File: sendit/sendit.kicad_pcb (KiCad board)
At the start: 4 copper layers, 160.7 x 51.7 mm, 227 parts, among them J1 Conn_01x04_MountingPin, J10 USB_TYPE_C_16PIN, J14 Conn_02x05_Odd_Even, J16 Conn_02x05_Odd_Even, J2 Conn_02x09_Odd_Even, J21 Conn_02x05_Odd_Even, J23 Conn_02x05_Odd_Even, J27 Conn_02x05_Odd_Even, J29 Conn_02x05_Odd_Even, J34 Conn_02x05_Odd_Even, J36 Conn_02x05_Odd_Even, J42 Conn_02x05_Odd_Even, J44 Conn_02x05_Odd_Even, J49 Conn_02x05_Odd_Even, J51 Conn_02x05_Odd_Even, J56 Conn_02x05_Odd_Even, J58 Conn_02x05_Odd_Even, J6 Conn_02x05_Odd_Even, J8 Conn_02x05_Odd_Even, Q1 AO3400A, SW1 RESET, SW2 BOOT, U1 ESP32-S3-WROOM-1-N16R8, U2 USBLC6-2SC6, U3 SN74LV1T34DBV, U4 XC6210B332MR, U5 ADS1115IDGSR, U6 ADS1115IDGSR, U7 TPS7A2033PDBVR, U8 MT3608, U9 AP63205WU

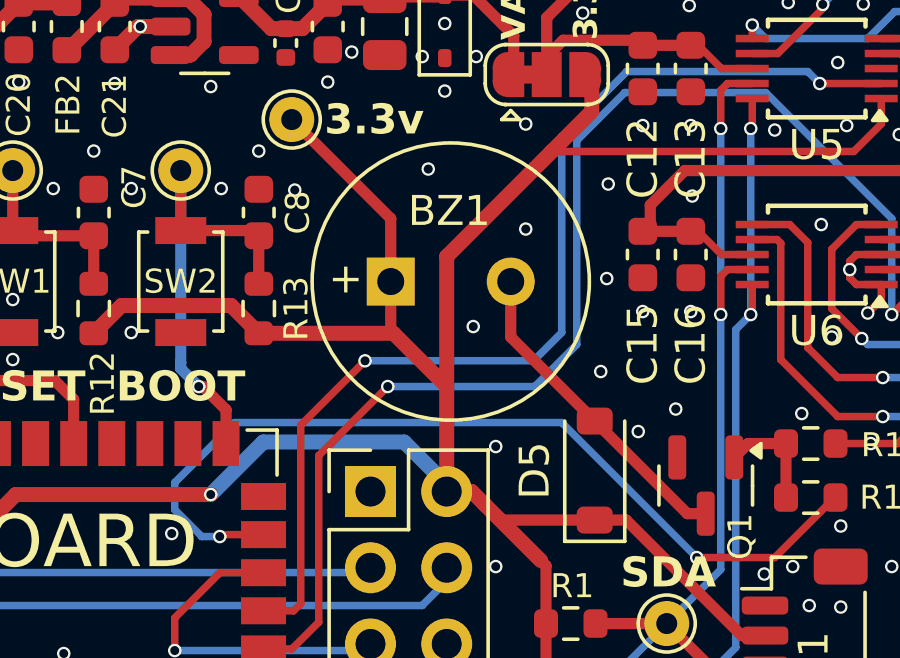
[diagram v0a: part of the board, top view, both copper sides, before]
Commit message: all footprints have 3d models now
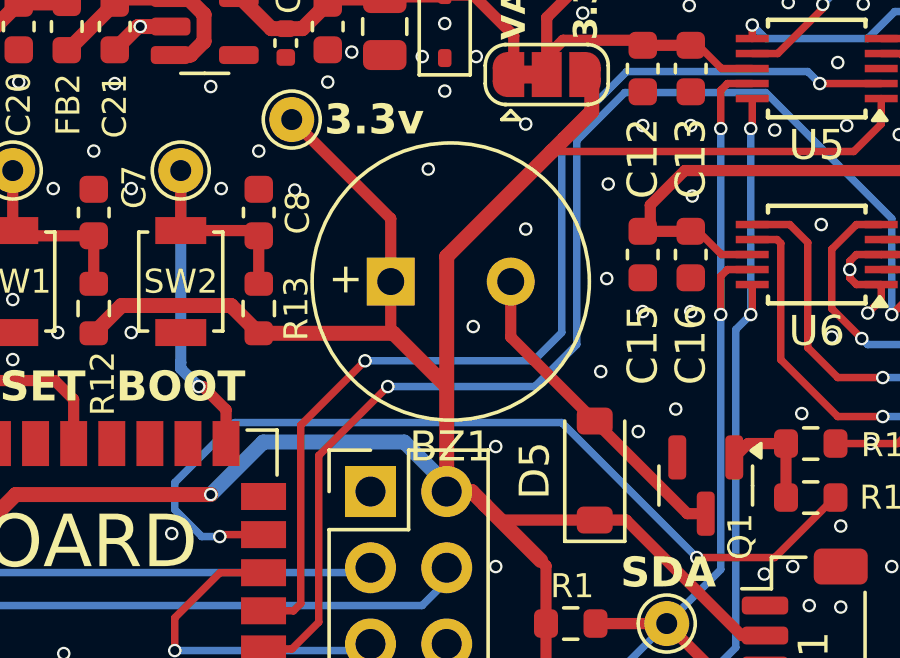
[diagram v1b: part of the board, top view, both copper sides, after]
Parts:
- BZ1: footprint Buzzer_Beeper:MagneticBuzzer_PUI_AT-0927-TT-6-R -> yarrboard:MagneticBuzzer_QMB-09B-03
- moved BZ1 2.00 mm to (91.5, 86.0)
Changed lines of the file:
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@@
 		)
 	)
-	(footprint "Buzzer_Beeper:MagneticBuzzer_PUI_AT-0927-TT-6-R"
+	(footprint "yarrboard:MagneticBuzzer_QMB-09B-03"
 		(layer "F.Cu")
-		(at 89.5 86)
+		(at 91.5 86)
 		(descr "Buzzer Magnetic 9mm AT-0927-TT-6-R, http://www.puiaudio.com/pdf/AT-0927-TT-6-R.pdf")
 		(tags "Buzzer Magnetic 9mm AT-0927-TT-6-R")
 		(property "Reference" "BZ1"
-			(at 1.95 -2.35 0)
+			(at 0 5.5 0)
 			(layer "F.SilkS")
 			(effects
@@
 		)
 		(property "Value" "Buzzer"
-			(at 2 7 0)
+			(at 0 7 0)
 			(layer "F.Fab")
 			(effects
@@
 		(attr through_hole)
 		(fp_circle
-			(center 2 0)
-			(end 6.62 0)
+			(center 0 0)
+			(end 4.62 0)
 			(stroke
 				(width 0.12)
@@
 		)
 		(fp_circle
-			(center 2 0)
-			(end 6.75 0)
+			(center 0 0)
+			(end 4.75 0)
 			(stroke
 				(width 0.05)
@@
 		)
 		(fp_circle
-			(center 2 0)
-			(end 6.5 0)
+			(center 0 0)
+			(end 4.5 0)
 			(stroke
 				(width 0.1)
@@
 		)
 		(fp_text user "+"
-			(at -1.5 -0.1 0)
+			(at -3.5 -0.1 0)
 			(layer "F.SilkS")
 			(effects
@@
 		)
 		(fp_text user "+"
-			(at -1.5 -0.1 0)
+			(at -3.5 -0.1 0)
 			(layer "F.Fab")
 			(effects
@@
 		)
 		(fp_text user "${REFERENCE}"
-			(at 2 2 0)
+			(at 0 2 0)
 			(layer "F.Fab")
 			(effects
@@
 		)
 		(pad "1" thru_hole rect
-			(at 0 0)
+			(at -2 0)
 			(size 1.6 1.6)
 			(drill 0.9)
@@
 		)
 		(pad "2" thru_hole circle
-			(at 4 0)
+			(at 2 0)
 			(size 1.6 1.6)
 			(drill 0.9)
@@
 		)
 		(embedded_fonts no)
-		(model "${KICAD9_3DMODEL_DIR}/Buzzer_Beeper.3dshapes/MagneticBuzzer_PUI_AT-0927-TT-6-R.step"
+		(model "/Users/hoeken/github/yarrboard-hardware/models/Huaneng QMB-09B-03.step"
 			(offset
 				(xyz 0 0 0)

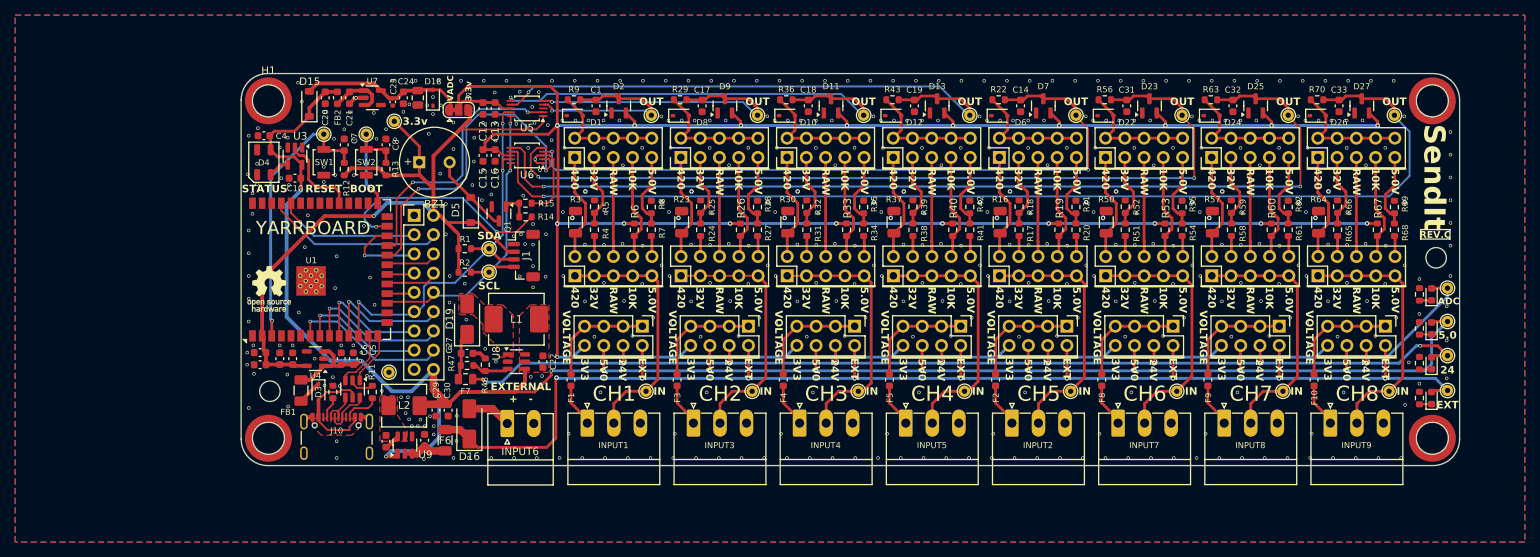
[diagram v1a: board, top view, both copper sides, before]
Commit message: moved the dc buck circuit away from the usb port.
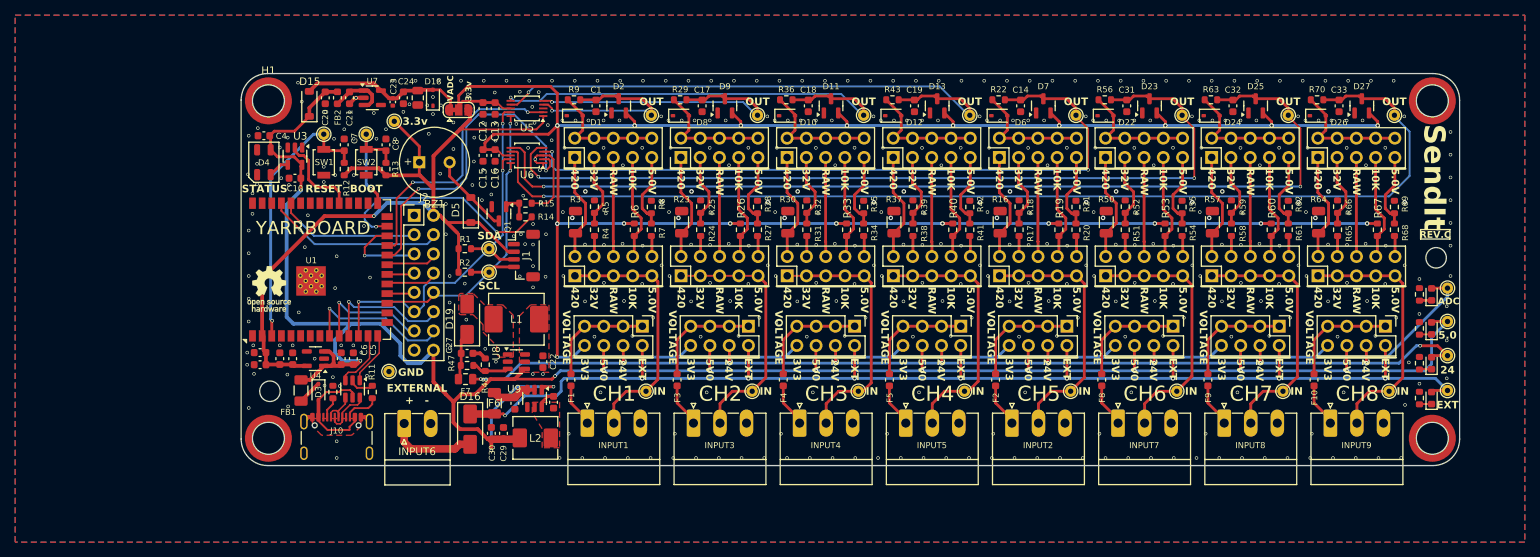
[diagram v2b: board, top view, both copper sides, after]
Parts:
- J2: footprint Connector_PinHeader_2.54mm:PinHeader_2x09_P2.54mm_Vertical -> Connector_PinHeader_2.54mm:PinHeader_2x08_P2.54mm_Vertical
- moved C28 22.7 mm to (107.2, 117.6), turned to 90 degrees
- moved U9 18.2 mm to (104.7, 117.1), turned to -90 degrees
- moved L2 17.8 mm to (104.8, 122.3), turned to 180 degrees
- moved INPUT6 13.6 mm to (87.5, 120.5)
- moved C26 12.9 mm to (102.1, 117.8), turned to -90 degrees
- moved C29 9.41 mm to (100.6, 121.7), turned to 90 degrees
- moved F6 8.13 mm to (99.4, 117.8), turned to 90 degrees
- moved C30 6.46 mm to (99.0, 121.7), turned to 90 degrees
- moved D16 0.71 mm to (96.2, 121.2), turned to -90 degrees
- moved TP19 0.10 mm to (85.5, 113.6)
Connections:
- J2 pad 15: GPIO15 -> GND
- J2 pad 16: GPIO7 -> +5V
- U1 pad 7: GPIO7 -> /ESP32-S3/GPIO7
- U1 pad 8: GPIO15 -> /ESP32-S3/GPIO15
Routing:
- net GPIO7: track 20.6 -> 0.00 mm, vias 1 -> 0
- net +5V: track 271.7 -> 291.3 mm
- net GPIO15: track 16.7 -> 0.00 mm, vias 1 -> 0
- net VEXT: track 179.3 -> 169.4 mm
- net Net-(D16-A): track 5.81 -> 11.8 mm
- net /Power Supply/bst: track 2.00 -> 2.51 mm
- net GND: vias 482 -> 461
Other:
- board text added: "GND"

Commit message: some bom work
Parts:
- C22: value 22uF / 10v -> 22uF
- C26: value 10uF / 50v -> 10uF / 35v
- C27: value 22uF / 50v -> 22uF / 35v; footprint Capacitor_SMD:C_0603_1608Metric -> Capacitor_SMD:C_0805_2012Metric
- moved D19 0.40 mm to (95.8, 106.3)
- moved C27 0.28 mm to (95.6, 111.0)
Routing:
- net Net-(D19-K): track 5.86 -> 7.44 mm
- net GND: vias 461 -> 485
